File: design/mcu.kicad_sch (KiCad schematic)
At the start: 35 parts, among them J2 SWD_01X04, J3 DEBUG_SPI, U6 STM32H750VBTx, X1 ASTX-H11-25.000MHZ-T, X2 SIT8209AI-21-33S-100.000000X

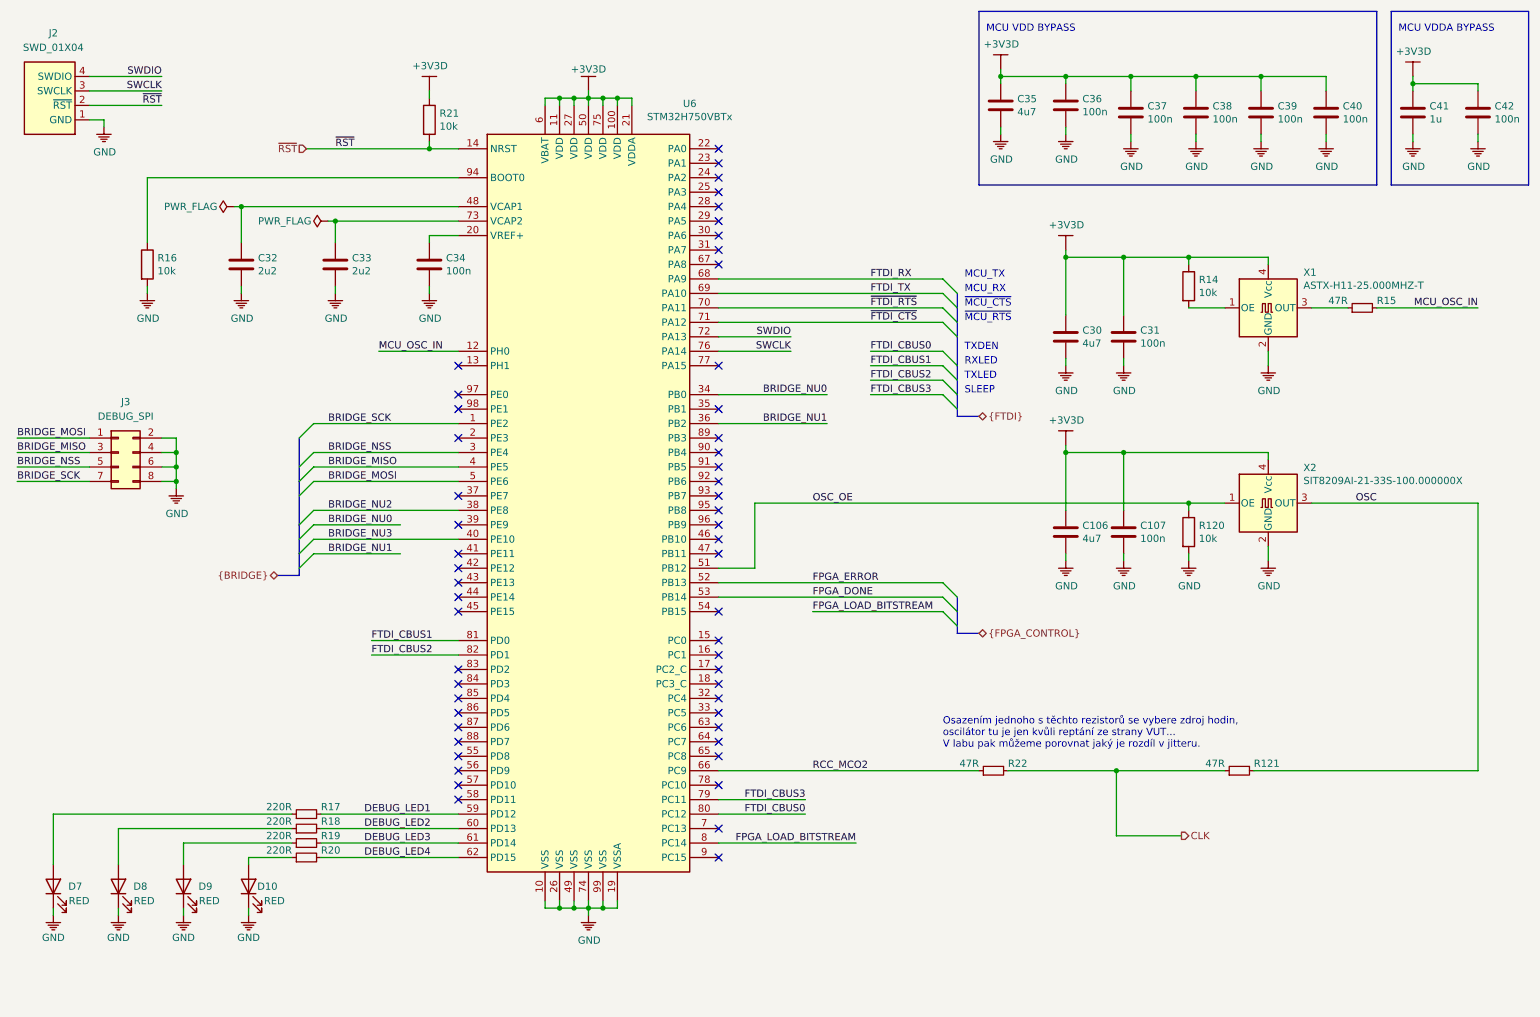
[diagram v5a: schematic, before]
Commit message: Fixed MCU RST
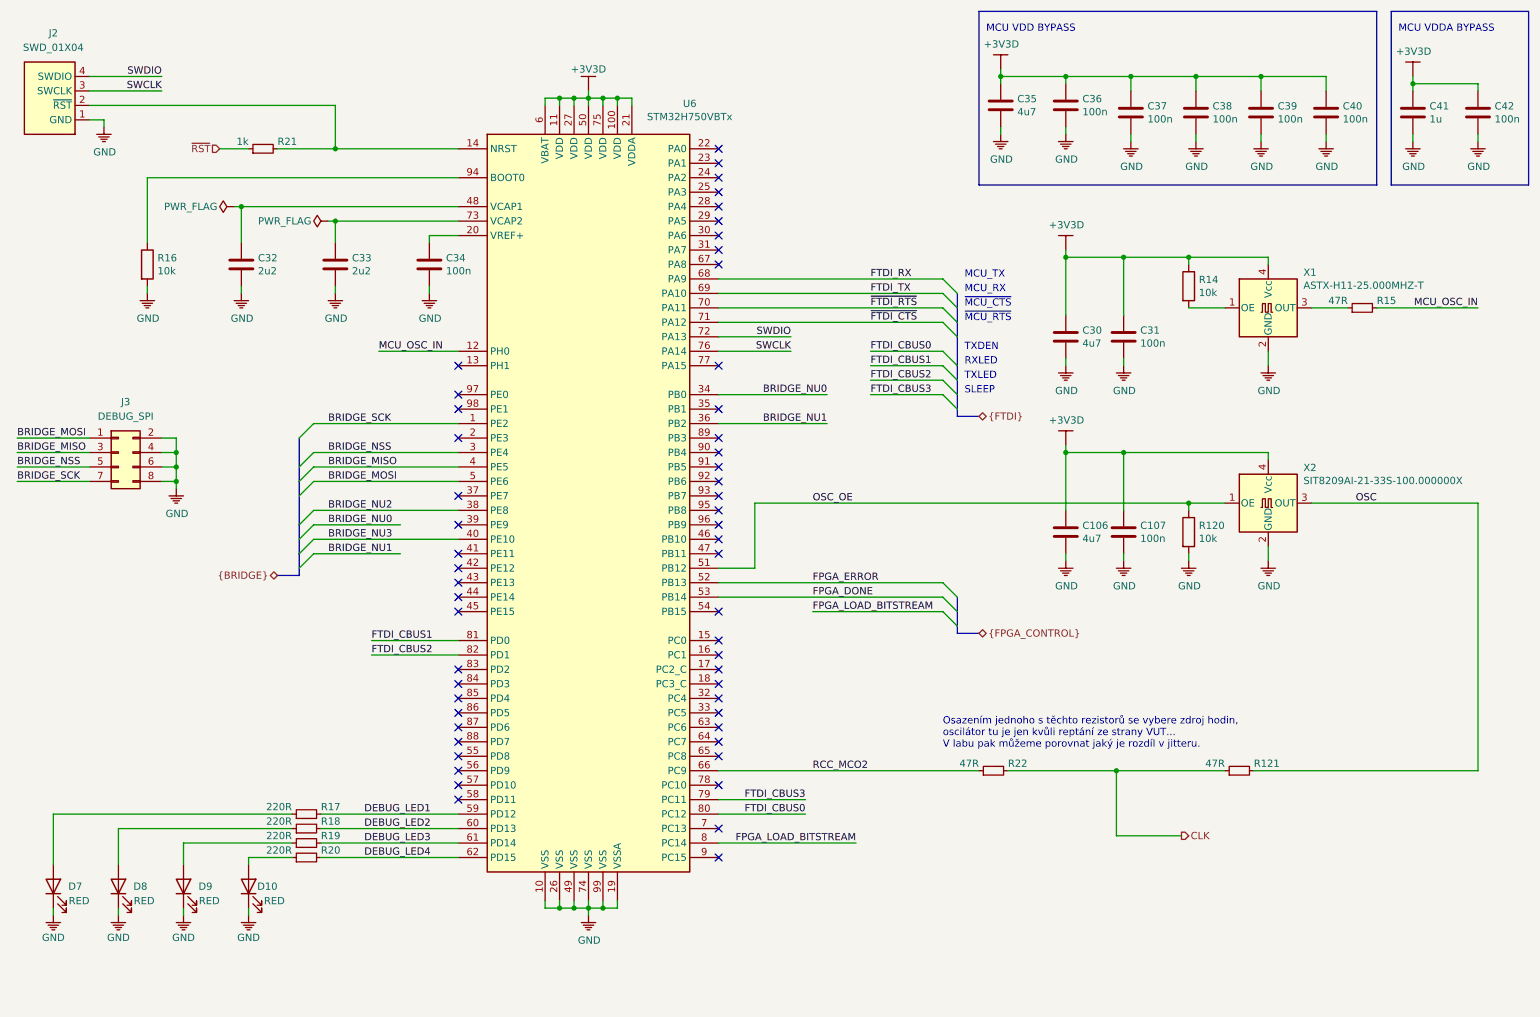
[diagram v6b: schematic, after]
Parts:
- removed R21: 10k, Resistor_SMD:R_0603_1608Metric, symbol Device:R
- added R21: 1k, Resistor_SMD:R_0603_1608Metric, symbol Device:R_Small
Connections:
- net ~RST: now also R21.1; no longer J2.2 (~RST), U6.14 (NRST)
- new net: J2.2 (~RST), R21.2, U6.14 (NRST)
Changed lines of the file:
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@@
   (junction (at 45.72 96.52))
   (junction (at 57.15 48.26))
+  (junction (at 73.66 38.1))
   (junction (at 73.66 50.8))
-  (junction (at 90.17 38.1))
   (junction (at 113.03 29.21))
   (junction (at 113.03 171.45))
@@
   (junction (at 236.22 25.4))
   (junction (at 262.89 26.67))
+  (no_connect (at 140.97 43.18))
+  (no_connect (at 140.97 134.62))
+  (no_connect (at 140.97 124.46))
+  (no_connect (at 95.25 139.7))
+  (no_connect (at 140.97 53.34))
+  (no_connect (at 140.97 88.9))
   (no_connect (at 140.97 55.88))
+  (no_connect (at 140.97 45.72))
+  (no_connect (at 140.97 142.24))
+  (no_connect (at 140.97 137.16))
+  (no_connect (at 95.25 144.78))
+  (no_connect (at 95.25 142.24))
+  (no_connect (at 140.97 40.64))
+  (no_connect (at 140.97 109.22))
+  (no_connect (at 140.97 139.7))
+  (no_connect (at 95.25 111.76))
+  (no_connect (at 140.97 38.1))
+  (no_connect (at 95.25 88.9))
+  (no_connect (at 140.97 162.56))
+  (no_connect (at 95.25 147.32))
+  (no_connect (at 140.97 96.52))
+  (no_connect (at 140.97 132.08))
+  (no_connect (at 95.25 116.84))
+  (no_connect (at 140.97 50.8))
+  (no_connect (at 140.97 104.14))
+  (no_connect (at 140.97 93.98))
+  (no_connect (at 95.25 152.4))
+  (no_connect (at 95.25 149.86))
+  (no_connect (at 140.97 58.42))
+  (no_connect (at 95.25 83.82))
+  (no_connect (at 140.97 99.06))
+  (no_connect (at 140.97 101.6))
+  (no_connect (at 140.97 149.86))
+  (no_connect (at 140.97 83.82))
+  (no_connect (at 140.97 129.54))
+  (no_connect (at 95.25 137.16))
+  (no_connect (at 140.97 119.38))
+  (no_connect (at 95.25 119.38))
+  (no_connect (at 140.97 106.68))
+  (no_connect (at 140.97 91.44))
+  (no_connect (at 95.25 134.62))
+  (no_connect (at 95.25 114.3))
+  (no_connect (at 95.25 109.22))
+  (no_connect (at 140.97 127))
+  (no_connect (at 95.25 76.2))
+  (no_connect (at 140.97 157.48))
+  (no_connect (at 140.97 48.26))
+  (no_connect (at 95.25 104.14))
+  (no_connect (at 95.25 132.08))
+  (no_connect (at 140.97 76.2))
+  (no_connect (at 95.25 99.06))
   (no_connect (at 95.25 81.28))
-  (no_connect (at 140.97 83.82))
-  (no_connect (at 95.25 134.62))
-  (no_connect (at 140.97 104.14))
-  (no_connect (at 140.97 99.06))
-  (no_connect (at 140.97 157.48))
-  (no_connect (at 95.25 83.82))
-  (no_connect (at 140.97 106.68))
-  (no_connect (at 95.25 114.3))
-  (no_connect (at 140.97 48.26))
-  (no_connect (at 95.25 152.4))
-  (no_connect (at 140.97 119.38))
-  (no_connect (at 140.97 76.2))
-  (no_connect (at 95.25 144.78))
-  (no_connect (at 95.25 104.14))
-  (no_connect (at 95.25 119.38))
-  (no_connect (at 140.97 134.62))
-  (no_connect (at 140.97 53.34))
-  (no_connect (at 140.97 43.18))
-  (no_connect (at 140.97 50.8))
-  (no_connect (at 140.97 88.9))
-  (no_connect (at 95.25 99.06))
-  (no_connect (at 140.97 139.7))
-  (no_connect (at 95.25 116.84))
-  (no_connect (at 140.97 58.42))
-  (no_connect (at 140.97 91.44))
   (no_connect (at 140.97 144.78))
-  (no_connect (at 95.25 147.32))
-  (no_connect (at 140.97 137.16))
-  (no_connect (at 140.97 149.86))
-  (no_connect (at 140.97 38.1))
-  (no_connect (at 95.25 109.22))
-  (no_connect (at 140.97 93.98))
-  (no_connect (at 95.25 149.86))
-  (no_connect (at 140.97 101.6))
-  (no_connect (at 140.97 109.22))
-  (no_connect (at 140.97 129.54))
-  (no_connect (at 95.25 88.9))
-  (no_connect (at 140.97 142.24))
-  (no_connect (at 95.25 132.08))
-  (no_connect (at 140.97 162.56))
-  (no_connect (at 95.25 76.2))
-  (no_connect (at 95.25 111.76))
   (no_connect (at 95.25 129.54))
-  (no_connect (at 140.97 40.64))
-  (no_connect (at 140.97 96.52))
-  (no_connect (at 95.25 137.16))
-  (no_connect (at 95.25 142.24))
-  (no_connect (at 140.97 124.46))
-  (no_connect (at 140.97 132.08))
-  (no_connect (at 140.97 45.72))
-  (no_connect (at 95.25 139.7))
-  (no_connect (at 140.97 127))
   (bus_entry (at 67.31 88.9) (size 2.54 -2.54))
   (bus_entry (at 67.31 93.98) (size 2.54 -2.54))
@@
   (wire (pts (xy 30.48 25.4) (xy 43.18 25.4)))
   (wire (pts (xy 30.48 27.94) (xy 43.18 27.94)))
-  (wire (pts (xy 30.48 30.48) (xy 43.18 30.48)))
+  (wire (pts (xy 30.48 30.48) (xy 73.66 30.48)))
   (wire (pts (xy 30.48 33.02) (xy 33.02 33.02)))
   (wire (pts (xy 33.02 33.02) (xy 33.02 34.29)))
@@
   (wire (pts (xy 46.99 160.02) (xy 46.99 163.83)))
   (wire (pts (xy 46.99 171.45) (xy 46.99 172.72)))
+  (wire (pts (xy 53.34 38.1) (xy 58.42 38.1)))
   (wire (pts (xy 55.88 48.26) (xy 57.15 48.26)))
   (wire (pts (xy 57.15 48.26) (xy 57.15 54.61)))
@@
   (wire (pts (xy 58.42 162.56) (xy 58.42 163.83)))
   (wire (pts (xy 58.42 171.45) (xy 58.42 172.72)))
+  (wire (pts (xy 63.5 38.1) (xy 73.66 38.1)))
   (wire (pts (xy 66.04 154.94) (xy 24.13 154.94)))
   (wire (pts (xy 66.04 157.48) (xy 35.56 157.48)))
   (wire (pts (xy 66.04 160.02) (xy 46.99 160.02)))
   (wire (pts (xy 66.04 162.56) (xy 58.42 162.56)))
-  (wire (pts (xy 68.58 38.1) (xy 90.17 38.1)))
   (wire (pts (xy 69.85 86.36) (xy 95.25 86.36)))
   (wire (pts (xy 69.85 91.44) (xy 95.25 91.44)))
@@
   (wire (pts (xy 69.85 109.22) (xy 85.09 109.22)))
   (wire (pts (xy 72.39 50.8) (xy 73.66 50.8)))
+  (wire (pts (xy 73.66 30.48) (xy 73.66 38.1)))
+  (wire (pts (xy 73.66 38.1) (xy 95.25 38.1)))
   (wire (pts (xy 73.66 50.8) (xy 73.66 54.61)))
   (wire (pts (xy 73.66 50.8) (xy 95.25 50.8)))
@@
   (wire (pts (xy 80.01 127) (xy 95.25 127)))
   (wire (pts (xy 81.28 73.66) (xy 95.25 73.66)))
-  (wire (pts (xy 90.17 27.94) (xy 90.17 29.21)))
-  (wire (pts (xy 90.17 38.1) (xy 90.17 36.83)))
-  (wire (pts (xy 90.17 38.1) (xy 95.25 38.1)))
   (wire (pts (xy 90.17 53.34) (xy 95.25 53.34)))
   (wire (pts (xy 90.17 54.61) (xy 90.17 53.34)))
@@
   (bus (pts (xy 182.88 81.28) (xy 182.88 85.09)))
   (bus (pts (xy 182.88 85.09) (xy 186.69 85.09)))
-  (bus (pts (xy 182.88 116.84) (xy 182.88 119.38)))
-  (bus (pts (xy 182.88 119.38) (xy 182.88 123.19)))
+  (bus (pts (xy 182.88 116.84) (xy 182.88 121.92)))
+  (bus (pts (xy 182.88 121.92) (xy 182.88 123.19)))
   (bus (pts (xy 186.69 123.19) (xy 182.88 123.19)))
   (polyline (pts (xy 186.69 13.97) (xy 186.69 44.45)))
@@
     (effects (font (size 1.27 1.27)) (justify right bottom))
   )
-  (label "~RST" (at 43.18 30.48 180)
-    (effects (font (size 1.27 1.27)) (justify right bottom))
-  )
   (label "BRIDGE_SCK" (at 72.39 86.36 0)
     (effects (font (size 1.27 1.27)) (justify left bottom))
@@
     (effects (font (size 1.27 1.27)) (justify left bottom))
   )
-  (label "~RST" (at 73.66 38.1 0)
-    (effects (font (size 1.27 1.27)) (justify left bottom))
-  )
   (label "DEBUG_LED1" (at 78.74 154.94 0)
     (effects (font (size 1.27 1.27)) (justify left bottom))
@@
   (label "MCU_OSC_IN" (at 274.32 66.04 180)
     (effects (font (size 1.27 1.27)) (justify right bottom))
+  )
+  (hierarchical_label "~RST" (shape input) (at 53.34 38.1 180)
+    (effects (font (size 1.27 1.27)) (justify right))
   )
   (hierarchical_label "{BRIDGE}" (shape bidirectional) (at 63.5 113.03 180)
     (effects (font (size 1.27 1.27)) (justify right))
   )
-  (hierarchical_label "~RST" (shape input) (at 68.58 38.1 180)
-    (effects (font (size 1.27 1.27)) (justify right))
-  )
   (hierarchical_label "{FTDI}" (shape bidirectional) (at 186.69 85.09 0)
     (effects (font (size 1.27 1.27)) (justify left))
@@
     )
   )
-  (symbol (lib_id "KLIB_Power:+3V3D") (at 90.17 27.94 0) (unit 1)
-    (property "Reference" "#PWR071" (id 0) (at 90.17 35.56 0)
-      (effects (font (size 1.27 1.27)) hide)
-    )
-    (property "Value" "+3V3D" (id 1) (at 90.297 23.5458 0))
-    (property "Footprint" "" (id 2) (at 90.17 27.94 0)
-      (effects (font (size 1.27 1.27)) hide)
-    )
-    (property "Datasheet" "" (id 3) (at 90.17 27.94 0)
-      (effects (font (size 1.27 1.27)) hide)
-    )
-  )
   (symbol (lib_id "KLIB_Power:GND") (at 90.17 63.5 0) (unit 1)
     (property "Reference" "#PWR072" (id 0) (at 90.17 68.58 0)
@@
     )
     (property "Datasheet" "" (id 3) (at 274.32 36.83 0)
+      (effects (font (size 1.27 1.27)) hide)
+    )
+  )
+  (symbol (lib_name "Device:R_Small_1") (lib_id "Device:R_Small") (at 60.96 38.1 90) (unit 1)
+    (property "Reference" "R21" (id 0) (at 63.5 36.83 90)
+      (effects (font (size 1.27 1.27)) (justify right))
+    )
+    (property "Value" "1k" (id 1) (at 58.42 36.83 90)
+      (effects (font (size 1.27 1.27)) (justify left))
+    )
+    (property "Footprint" "Resistor_SMD:R_0603_1608Metric" (id 2) (at 60.96 38.1 0)
+      (effects (font (size 1.27 1.27)) hide)
+    )
+    (property "Datasheet" "~" (id 3) (at 60.96 38.1 0)
       (effects (font (size 1.27 1.27)) hide)
     )
@@
       (effects (font (size 1.27 1.27)) hide)
     )
-  )
-  (symbol (lib_id "Device:R") (at 90.17 33.02 0) (unit 1)
-    (property "Reference" "R21" (id 0) (at 91.948 31.877 0)
-      (effects (font (size 1.27 1.27)) (justify left))
-    )
-    (property "Value" "10k" (id 1) (at 91.948 34.163 0)
-      (effects (font (size 1.27 1.27)) (justify left))
-    )
-    (property "Footprint" "Resistor_SMD:R_0603_1608Metric" (id 2) (at 88.392 33.02 90)
-      (effects (font (size 1.27 1.27)) hide)
-    )
-    (property "Datasheet" "~" (id 3) (at 90.17 33.02 0)
-      (effects (font (size 1.27 1.27)) hide)
-    )

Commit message: Updated some layout
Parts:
- renumbered C32 to C30, C33 to C31, C34 to C32, C35 to C33, C36 to C34, C30 to C35, C106 to C36, C31 to C37, C107 to C38, C37 to C39, C38 to C40, C39 to C41, C40 to C42, C41 to C43, C42 to C44, R16 to R14, R21 to R15, R17 to R16, R18 to R17, R19 to R18, R20 to R19, R22 to R20, R14 to R21, R120 to R22, R121 to R23, R15 to R24

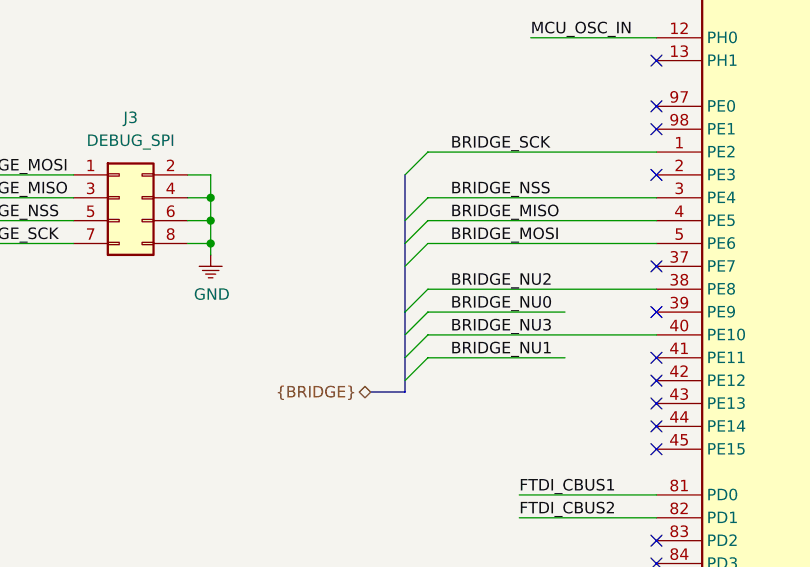
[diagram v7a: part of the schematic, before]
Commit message: Added logo and description to F.Silks
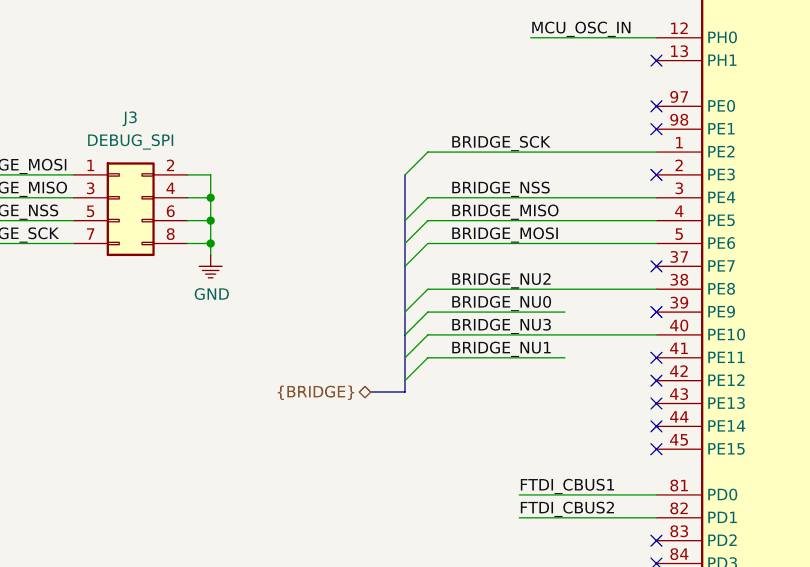
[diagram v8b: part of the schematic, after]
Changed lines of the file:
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@@
-(kicad_sch (version 20200512) (host eeschema "5.99.0-unknown-d72a778~101~ubuntu18.04.1")
+(kicad_sch (version 20200512) (host eeschema "5.99.0-unknown-4efed4b~101~ubuntu18.04.1")
   (page 3 8)
   (paper "A4")
@@
   (junction (at 236.22 25.4))
   (junction (at 262.89 26.67))
+  (no_connect (at 140.97 91.44))
+  (no_connect (at 140.97 48.26))
+  (no_connect (at 95.25 99.06))
+  (no_connect (at 95.25 144.78))
   (no_connect (at 140.97 43.18))
+  (no_connect (at 95.25 152.4))
+  (no_connect (at 140.97 83.82))
+  (no_connect (at 95.25 132.08))
+  (no_connect (at 140.97 40.64))
+  (no_connect (at 95.25 114.3))
+  (no_connect (at 95.25 116.84))
+  (no_connect (at 140.97 76.2))
+  (no_connect (at 140.97 129.54))
+  (no_connect (at 95.25 88.9))
+  (no_connect (at 140.97 45.72))
+  (no_connect (at 95.25 137.16))
+  (no_connect (at 140.97 96.52))
+  (no_connect (at 95.25 129.54))
+  (no_connect (at 95.25 149.86))
+  (no_connect (at 95.25 142.24))
   (no_connect (at 140.97 134.62))
+  (no_connect (at 140.97 58.42))
+  (no_connect (at 95.25 76.2))
+  (no_connect (at 95.25 134.62))
+  (no_connect (at 140.97 144.78))
+  (no_connect (at 95.25 81.28))
+  (no_connect (at 140.97 127))
+  (no_connect (at 95.25 139.7))
+  (no_connect (at 140.97 104.14))
+  (no_connect (at 140.97 162.56))
   (no_connect (at 140.97 124.46))
-  (no_connect (at 95.25 139.7))
-  (no_connect (at 140.97 53.34))
-  (no_connect (at 140.97 88.9))
-  (no_connect (at 140.97 55.88))
-  (no_connect (at 140.97 45.72))
+  (no_connect (at 95.25 83.82))
+  (no_connect (at 140.97 109.22))
+  (no_connect (at 140.97 38.1))
+  (no_connect (at 140.97 99.06))
+  (no_connect (at 140.97 93.98))
+  (no_connect (at 140.97 137.16))
+  (no_connect (at 140.97 106.68))
   (no_connect (at 140.97 142.24))
-  (no_connect (at 140.97 137.16))
-  (no_connect (at 95.25 144.78))
-  (no_connect (at 95.25 142.24))
-  (no_connect (at 140.97 40.64))
-  (no_connect (at 140.97 109.22))
-  (no_connect (at 140.97 139.7))
-  (no_connect (at 95.25 111.76))
-  (no_connect (at 140.97 38.1))
-  (no_connect (at 95.25 88.9))
-  (no_connect (at 140.97 162.56))
-  (no_connect (at 95.25 147.32))
-  (no_connect (at 140.97 96.52))
-  (no_connect (at 140.97 132.08))
-  (no_connect (at 95.25 116.84))
   (no_connect (at 140.97 50.8))
-  (no_connect (at 140.97 104.14))
-  (no_connect (at 140.97 93.98))
-  (no_connect (at 95.25 152.4))
-  (no_connect (at 95.25 149.86))
-  (no_connect (at 140.97 58.42))
-  (no_connect (at 95.25 83.82))
-  (no_connect (at 140.97 99.06))
-  (no_connect (at 140.97 101.6))
+  (no_connect (at 95.25 104.14))
   (no_connect (at 140.97 149.86))
-  (no_connect (at 140.97 83.82))
-  (no_connect (at 140.97 129.54))
-  (no_connect (at 95.25 137.16))
   (no_connect (at 140.97 119.38))
   (no_connect (at 95.25 119.38))
-  (no_connect (at 140.97 106.68))
-  (no_connect (at 140.97 91.44))
-  (no_connect (at 95.25 134.62))
-  (no_connect (at 95.25 114.3))
+  (no_connect (at 140.97 157.48))
+  (no_connect (at 140.97 88.9))
+  (no_connect (at 95.25 147.32))
+  (no_connect (at 140.97 139.7))
+  (no_connect (at 140.97 55.88))
+  (no_connect (at 140.97 101.6))
+  (no_connect (at 95.25 111.76))
   (no_connect (at 95.25 109.22))
-  (no_connect (at 140.97 127))
-  (no_connect (at 95.25 76.2))
-  (no_connect (at 140.97 157.48))
-  (no_connect (at 140.97 48.26))
-  (no_connect (at 95.25 104.14))
-  (no_connect (at 95.25 132.08))
-  (no_connect (at 140.97 76.2))
-  (no_connect (at 95.25 99.06))
-  (no_connect (at 95.25 81.28))
-  (no_connect (at 140.97 144.78))
-  (no_connect (at 95.25 129.54))
+  (no_connect (at 140.97 132.08))
+  (no_connect (at 140.97 53.34))
   (bus_entry (at 67.31 88.9) (size 2.54 -2.54))
   (bus_entry (at 67.31 93.98) (size 2.54 -2.54))
@@
   (wire (pts (xy 274.32 100.33) (xy 274.32 147.32)))
   (bus (pts (xy 63.5 113.03) (xy 67.31 113.03)))
-  (bus (pts (xy 67.31 88.9) (xy 67.31 96.52)))
-  (bus (pts (xy 67.31 96.52) (xy 67.31 104.14)))
-  (bus (pts (xy 67.31 104.14) (xy 67.31 109.22)))
-  (bus (pts (xy 67.31 109.22) (xy 67.31 113.03)))
+  (bus (pts (xy 67.31 88.9) (xy 67.31 93.98)))
+  (bus (pts (xy 67.31 93.98) (xy 67.31 99.06)))
+  (bus (pts (xy 67.31 99.06) (xy 67.31 106.68)))
+  (bus (pts (xy 67.31 106.68) (xy 67.31 111.76)))
+  (bus (pts (xy 67.31 111.76) (xy 67.31 113.03)))
   (bus (pts (xy 182.88 63.5) (xy 182.88 68.58)))
   (bus (pts (xy 182.88 68.58) (xy 182.88 76.2)))
